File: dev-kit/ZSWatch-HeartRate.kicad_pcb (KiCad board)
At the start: 4 copper layers, 45 x 36.9 mm, 49 parts, among them IC101 LIS2DS12, IC102 MCP73832-2-OT, IC103 MAX32664, IC104 TPS61240, IC105 MAX86141, IC106 MIC5365-1.8, J101 SPI, J102 GPIO, J103 UART, J104 I2C, M101 BM15C, SW101 BTN1, SW102 RESET, X102 CHARGE, X103 BATTERY, X104 DEBUG, Y101 32kHz

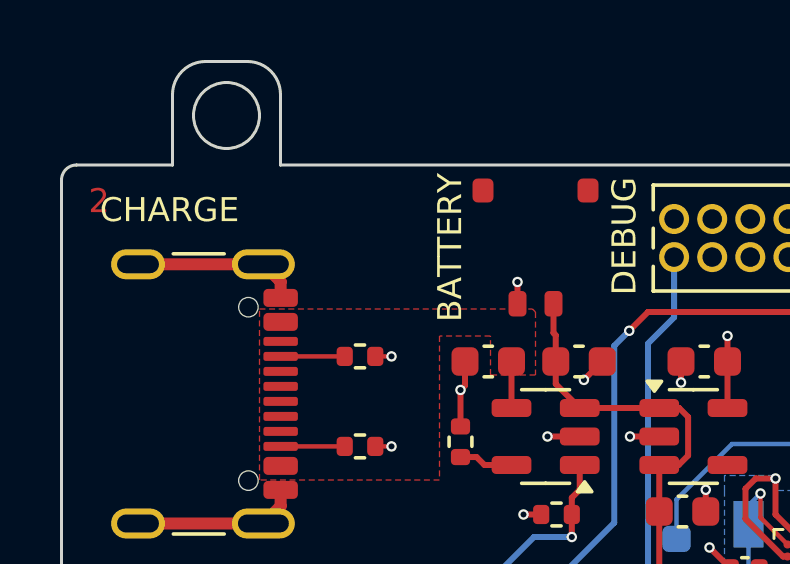
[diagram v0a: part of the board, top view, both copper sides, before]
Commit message: Start with hardware rev 3
- Fix distance between programming and battery connector

Signed-off-by: Daniel Kampert <DanielKampert@kampis-elektroecke.de>
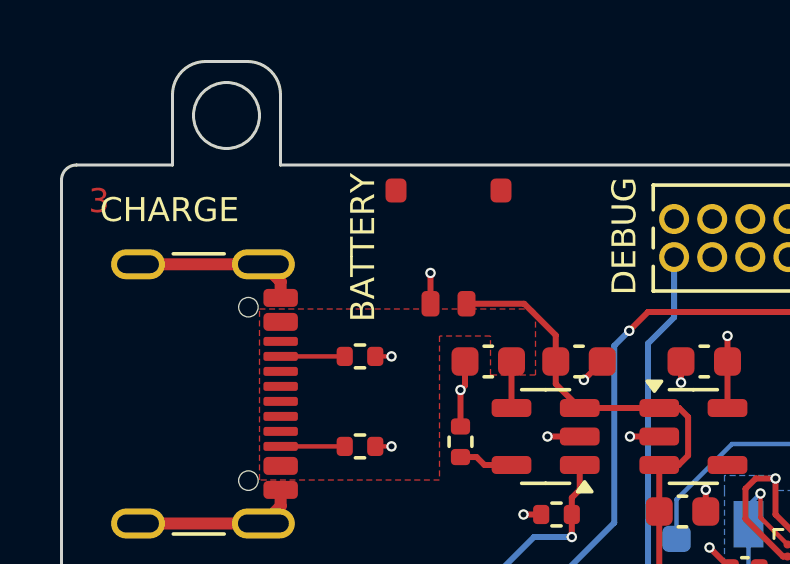
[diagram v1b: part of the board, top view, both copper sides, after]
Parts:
- moved X103 2.90 mm to (154.1, 90.5)
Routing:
- net /V_{BAT}: track 19.7 -> 22.0 mm
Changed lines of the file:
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@@
 	(paper "A4")
 	(title_block
-		(title "ZSWatch Heartrate")
-		(date "2025-04-18")
-		(rev "2")
+		(title "ZSWatch Heart Rate Dev-Board")
+		(date "2025-05-20")
+		(rev "3")
 		(company "github.com/...")
 	)
@@
 	(footprint "Molex:78171-0002"
 		(layer "F.Cu")
-		(at 157 90.55 180)
+		(at 154.1 90.55 180)
 		(descr "Molex Pico-EZmate series connector, 78171-0002 (http://www.molex.com/pdm_docs/sd/781710002_sd.pdf), generated with kicad-footprint-generator")
 		(tags "connector Molex Pico-EZmate side entry")
@@
 	)
 	(segment
-		(start 156.4 92.425)
-		(end 156.4 91.7)
-		(width 0.2)
-		(layer "F.Cu")
-		(net 1)
-	)
-	(segment
 		(start 165.92 99.25)
 		(end 165.92 98.25)
@@
 	)
 	(segment
+		(start 153.5 91.4)
+		(end 153.5 92.425)
+		(width 0.2)
+		(layer "F.Cu")
+		(net 1)
+	)
+	(segment
 		(start 168.18 103.45)
 		(end 168.18 102.75)
@@
 	)
 	(via
-		(at 156.4 91.7)
+		(at 153.5 91.4)
 		(size 0.35)
 		(drill 0.2)
@@
 	)
 	(segment
-		(start 157.675 95.1)
-		(end 158.475 95.9)
+		(start 157.675 93.475)
+		(end 157.675 94.35)
 		(width 0.2)
 		(layer "F.Cu")
@@
 	)
 	(segment
-		(start 157.6 92.425)
-		(end 157.6 93.4)
+		(start 157.675 95.1)
+		(end 158.475 95.9)
 		(width 0.2)
 		(layer "F.Cu")
@@
 	)
 	(segment
-		(start 157.675 93.475)
-		(end 157.675 94.35)
-		(width 0.2)
-		(layer "F.Cu")
-		(net 4)
-	)
-	(segment
 		(start 161.025 104.6)
 		(end 161.3 104.6)
@@
 	)
 	(segment
-		(start 157.6 93.4)
-		(end 157.675 93.475)
+		(start 154.7 92.425)
+		(end 156.625 92.425)
 		(width 0.2)
 		(layer "F.Cu")
@@
 		(width 0.2)
 		(layer "F.Cu")
+		(net 4)
+	)
+	(segment
+		(start 156.625 92.425)
+		(end 157.675 93.475)
+		(width 0.2)
+		(layer "F.Cu")

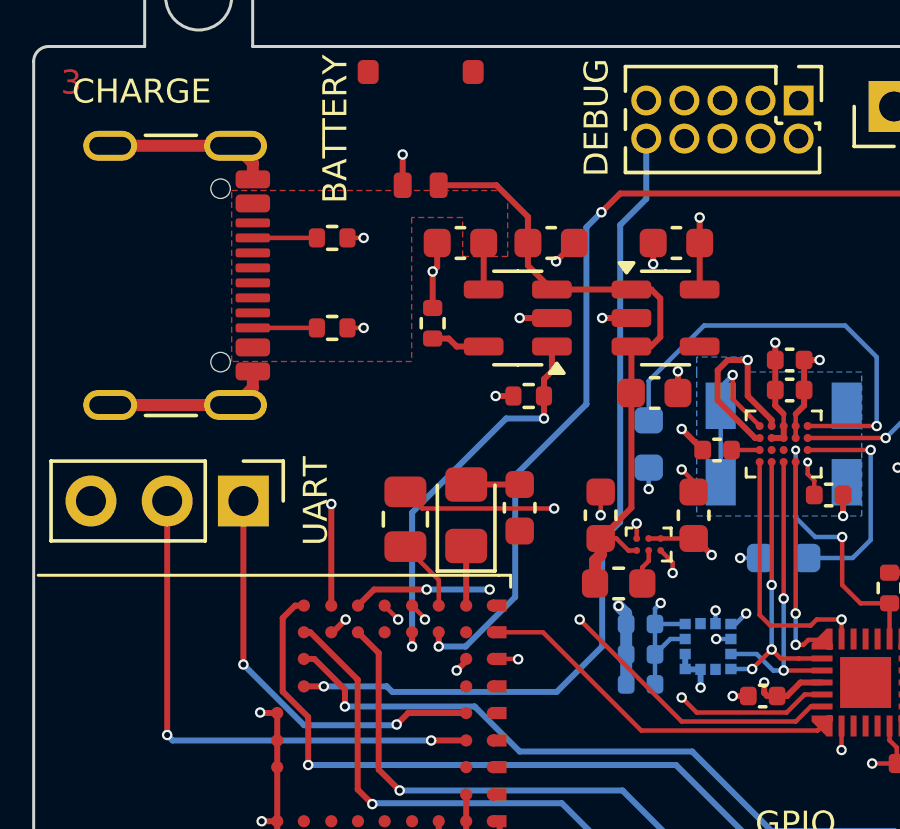
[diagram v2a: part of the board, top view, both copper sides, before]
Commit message: Bug: Issue #2
- Fix wrong circuit for the status LED

Signed-off-by: Daniel Kampert <DanielKampert@kampis-elektroecke.de>
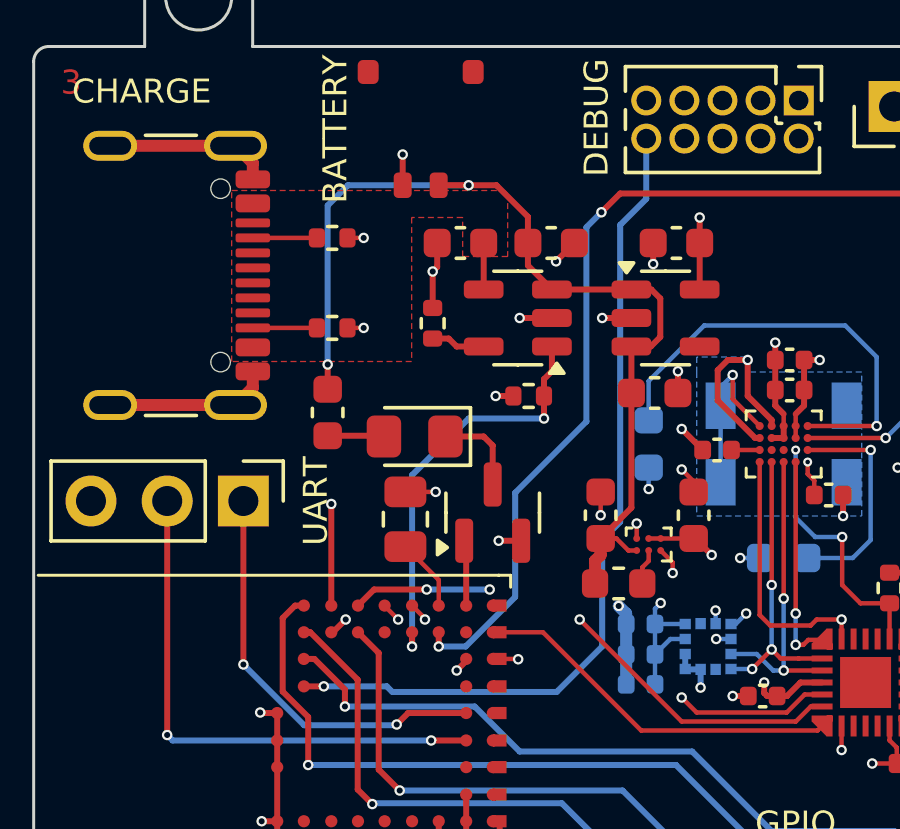
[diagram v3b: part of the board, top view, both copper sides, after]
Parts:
- added Q101: BSS138, Package_TO_SOT_SMD:SOT-23, F.Cu at (156.5, 103.3)
- moved R105 7.14 mm to (151.0, 100.0), turned to -90 degrees
- moved D107 3.14 mm to (153.9, 100.8), turned to 180 degrees
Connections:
- M101 pad K8: Net-(D107-K) -> Net-(M101-P2.05)
- R105 pad 1: +BATT -> /V_{BAT}
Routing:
- net /V_{BAT}: track 22.0 -> 33.3 mm, vias 0 -> 2
- net Net-(M101-P2.05): track 0.00 -> 2.19 mm
- net Net-(D107-K): track 1.99 -> 3.00 mm
- net GND: track 68.3 -> 69.0 mm, vias 31 -> 32
- net /CHARGE: track 13.1 -> 13.9 mm

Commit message: Issue #4
Signed-off-by: Daniel Kampert <DanielKampert@kampis-elektroecke.de>
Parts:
- moved C110 1.00 mm to (162.6, 93.3)
- moved C113 1.00 mm to (161.9, 98.3)
- moved IC106 1.00 mm to (162.3, 95.8)
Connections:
- D102 pad 2: GND -> PD_GND
- IC105 pad C5: GND -> PD_GND
- IC105 pad D4: GND -> Net-(D101-K)
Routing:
- net GND: track 69.0 -> 62.0 mm, vias 32 -> 31
- net /V_{BAT}: track 33.3 -> 34.6 mm
- net Net-(D105-K): track 14.7 -> 15.4 mm
- net Net-(D102-K): track 5.81 -> 5.19 mm
- net PD_GND: vias 0 -> 1
- added copper zone on B.Cu, net PD_GND
- added copper zone on F.Cu, net PD_GND
- added copper zone on In2.Cu, net PD_GND
- removed copper zone on In1.Cu, net (none)
- removed copper zone on B.Cu, net GND

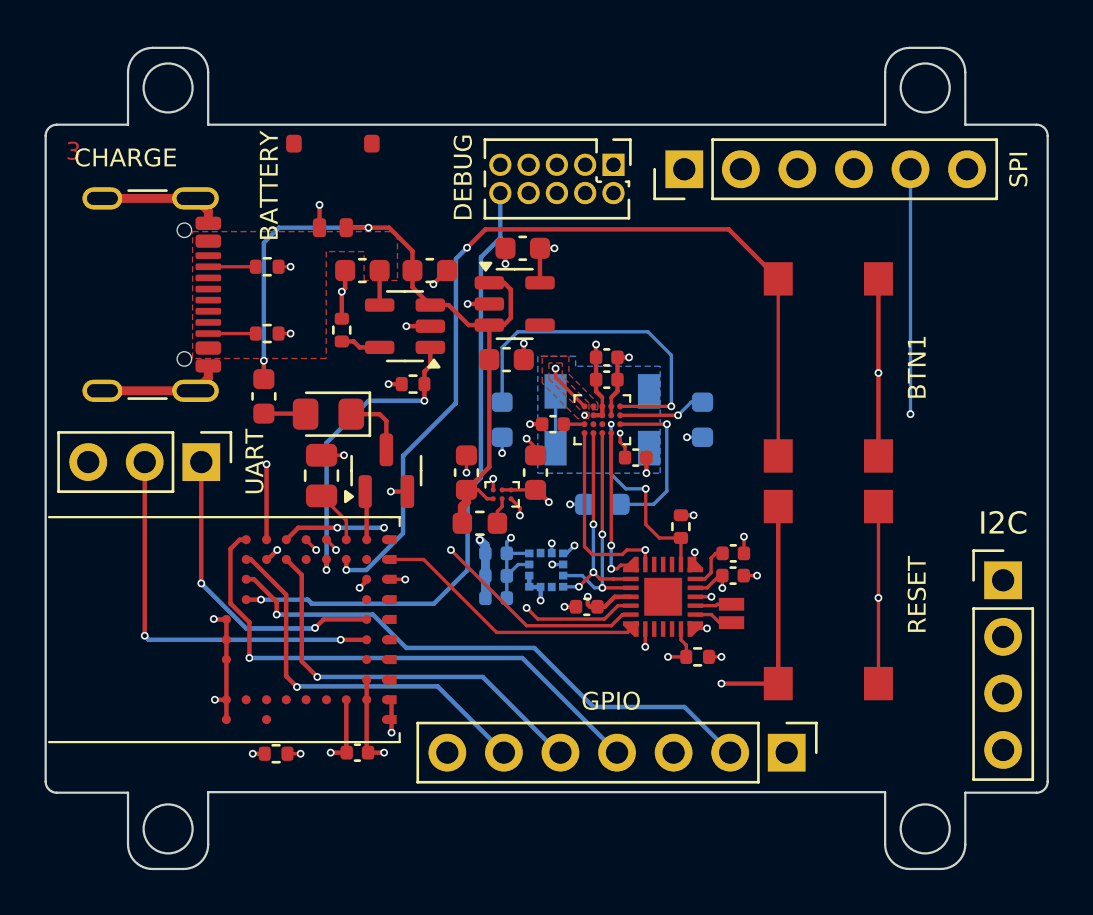
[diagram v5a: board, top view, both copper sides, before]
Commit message: Rework heartrate sensor
- Issue #7
- Issue #6
- Issue #5
- Issue #4

Signed-off-by: Daniel Kampert <DanielKampert@kampis-elektroecke.de>
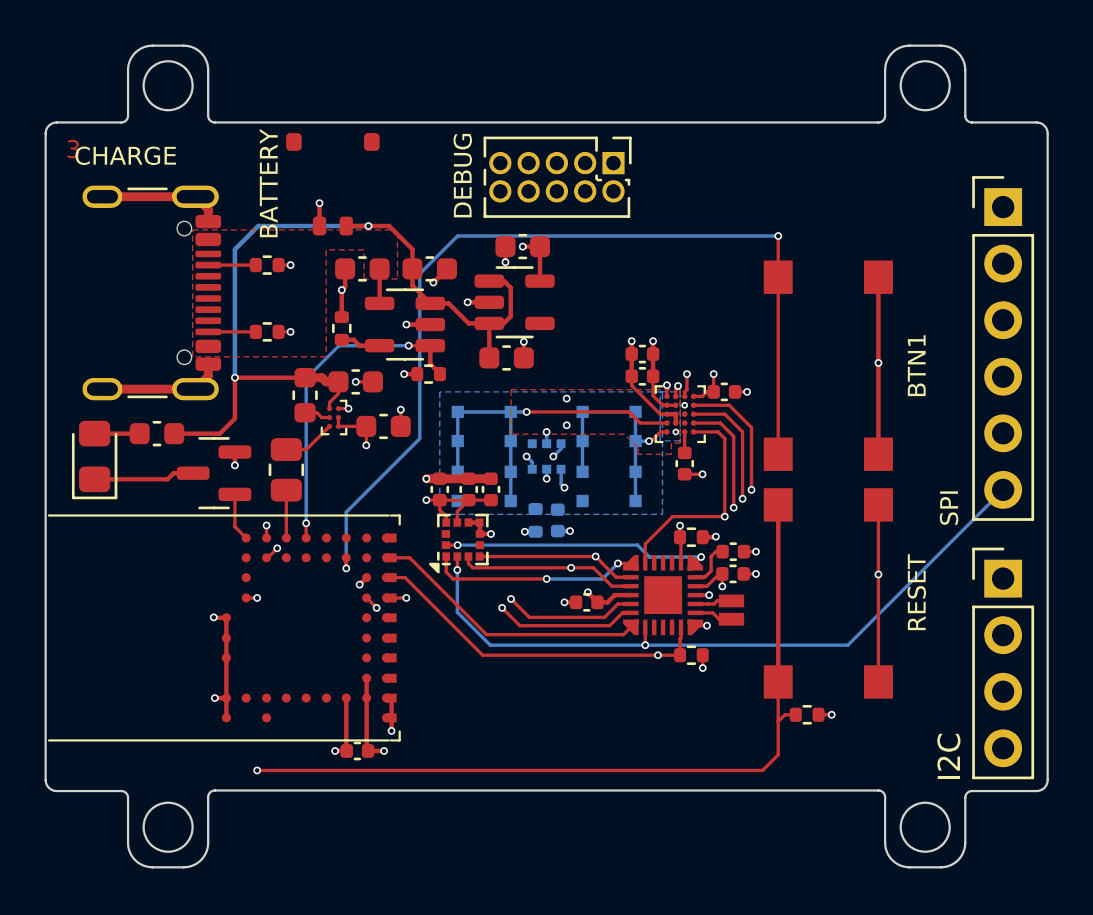
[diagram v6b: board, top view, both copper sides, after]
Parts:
- removed D104: IR, Diode_SMD:D_0603_1608Metric
- removed D105: GREEN, Diode_SMD:D_0603_1608Metric
- removed D106: RED, Diode_SMD:D_0603_1608Metric
- removed J102: GPIO, Connector_PinHeader_2.54mm:PinHeader_1x07_P2.54mm_Vertical
- removed J103: UART, Connector_PinHeader_2.54mm:PinHeader_1x03_P2.54mm_Vertical
- added C118: ~, Capacitor_SMD:C_0402_1005Metric, B.Cu at (164.2, 105.6)
- added D101: D_Photo, Vishay:VEMD8080, B.Cu at (160.9, 102.7)
- added LED101: SFH 7016, Osram:SFH7016, B.Cu at (163.7, 102.7)
- added R110: ~, Resistor_SMD:R_0402_1005Metric, B.Cu at (163.2, 105.6)
- C114, C115, C116, IC101: moved to F.Cu
- D102: footprint Vishay:VEMD5080X01 -> Vishay:VEMD8080
- moved R108 23.9 mm to (175.4, 114.3)
- moved J101 14.4 mm to (184.2, 91.5), turned to 0 degrees
- moved D107 10.7 mm to (143.4, 102.7), turned to 90 degrees
- moved L101 9.73 mm to (152.8, 100.0), turned to -90 degrees
- moved IC104 8.30 mm to (154.2, 101.0), turned to 0 degrees
- moved Q101 7.74 mm to (148.8, 103.5), turned to 180 degrees
- moved C108 7.13 mm to (156.4, 101.3), turned to 0 degrees
- moved C107 6.43 mm to (155.1, 99.3), turned to 0 degrees
- moved C104 6.18 mm to (169.9, 103.0), turned to -90 degrees
- moved R105 5.08 mm to (146.2, 101.7), turned to 180 degrees
- moved C106 4.95 mm to (171.7, 99.8)
- moved C115 4.89 mm to (161.2, 104.2), turned to 90 degrees
- moved C114 4.07 mm to (160.2, 104.2), turned to 90 degrees
- moved IC101 3.99 mm to (159.9, 106.4), turned to 90 degrees
- moved C116 3.83 mm to (158.9, 104.2), turned to 90 degrees
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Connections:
- J101 pad 2: Net-(IC101-SDA/SDI/SDO) -> Net-(IC101-SCL/SCLK)
- J101 pad 4: Net-(IC101-SCL/SCLK) -> Net-(IC101-SDA/SDI/SDO)
- J101 pad 5: Net-(IC101-CS) -> Net-(IC103-CS_{PPG})
- J101 pad 6: Net-(IC103-CS_{PPG}) -> Net-(IC101-CS)
- M101 pad E8: /TxD -> unconnected-(M101-P1.03/NFC-PadE8)
- M101 pad F8: Net-(J103-Pin_1) -> unconnected-(M101-P1.05/AIN1-PadF8)
- M101 pad G8: unconnected-(M101-P1.08-PadG8) -> /SCL
- M101 pad G9: unconnected-(M101-P1.07/AIN3-PadG9) -> /SDA
- M101 pad H2: Net-(J102-Pin_2) -> unconnected-(M101-P0.04-PadH2)
- M101 pad J2: Net-(J102-Pin_6) -> unconnected-(M101-P0.03-PadJ2)
- M101 pad J4: Net-(J102-Pin_5) -> unconnected-(M101-P0.00-PadJ4)
- M101 pad J6: /CHARGE -> unconnected-(M101-P2.07-PadJ6)
- M101 pad K2: Net-(J102-Pin_4) -> Net-(M101-P0.02)
- M101 pad K4: Net-(J102-Pin_3) -> Net-(M101-P0.01)
- M101 pad K5: /SDA -> /CHARGE
- M101 pad K6: /SCL -> unconnected-(M101-P2.08-PadK6)
- M101 pad K7: Net-(M101-P2.06) -> unconnected-(M101-P2.06-PadK7)
- M101 pad K8: Net-(M101-P2.05) -> unconnected-(M101-P2.05-PadK8)
- Q101 pad 1: Net-(M101-P2.05) -> Net-(M101-P0.02)
- R109 pad 1: Net-(M101-P2.06) -> Net-(M101-P0.01)
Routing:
- net Net-(J102-Pin_3): track 25.4 -> 0.00 mm, vias 2 -> 0
- net Net-(J102-Pin_2): track 25.3 -> 0.00 mm, vias 1 -> 0
- net Net-(J102-Pin_4): track 24.4 -> 0.00 mm, vias 1 -> 0
- net Net-(J102-Pin_5): track 18.2 -> 0.00 mm, vias 1 -> 0
- net /TxD: track 17.8 -> 0.00 mm, vias 2 -> 0
- net Net-(J102-Pin_6): track 17.3 -> 0.00 mm, vias 1 -> 0
- net Net-(D101-K): track 0.00 -> 16.3 mm, vias 0 -> 1
- net Net-(J103-Pin_1): track 13.9 -> 0.00 mm, vias 2 -> 0
- net Net-(IC101-SCL/SCLK): track 31.3 -> 41.6 mm
- net /ENABLE_{LED}: track 10.9 -> 2.37 mm, vias 2 -> 0
- net Net-(IC101-CS): track 39.7 -> 31.3 mm, vias 3 -> 2
- net /SCL: track 43.6 -> 35.6 mm
- net Net-(IC103-CS_{PPG}): track 31.8 -> 24.0 mm
- net Net-(IC105-LED1_DRV): track 15.4 -> 8.06 mm, vias 1 -> 2
- net Net-(IC101-SDO/ADDR0): track 31.0 -> 37.6 mm
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- added copper zone on In1.Cu, net +1V8
- added copper zone on In1.Cu, net /V_{LED}
- added copper zone on In2.Cu, net GND
- removed copper zone on In2.Cu, net +1V8
- removed copper zone on In2.Cu, net /V_{LED}
- removed copper zone on In1.Cu, net GND
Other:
- outline, holes or cut-outs redrawn

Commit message: Issue #8
Signed-off-by: Daniel Kampert <DanielKampert@kampis-elektroecke.de>
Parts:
- D101, D102: footprint Vishay:VEMD8080 -> Vishay:VEMD808x
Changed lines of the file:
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@@
 		)
 	)
-	(footprint "Vishay:VEMD8080"
+	(footprint "Vishay:VEMD808x"
 		(layer "B.Cu")
 		(at 166.5 102.7 -90)
@@
 			(unlocked yes)
 			(layer "B.SilkS")
-			(hide yes)
 			(effects
 				(font
@@
 			(unlocked yes)
 			(layer "B.Fab")
-			(hide yes)
-			(effects
-				(font
-					(size 1 1)
-					(thickness 0.15)
-				)
-				(justify mirror)
-			)
-		)
-		(property "Datasheet" "https://www.vishay.com/doc?84565"
+			(effects
+				(font
+					(size 1 1)
+					(thickness 0.15)
+				)
+				(justify mirror)
+			)
+		)
+		(property "Datasheet" "https://www.vishay.com/docs/80381/vemd8082.pdf"
 			(at 0 0 90)
 			(unlocked yes)
@@
 			)
 		)
-		(property "manf#" "VEMD8080"
+		(property "manf#" "VEMD8082"
 			(at 0 0 270)
 			(unlocked yes)
@@
 			)
 		)
-		(property "mouser#" "78-VEMD8080"
+		(property "mouser#" "78-VEMD8082"
 			(at 0 0 270)
 			(unlocked yes)
@@
 		)
 	)
-	(footprint "Vishay:VEMD8080"
+	(footprint "Vishay:VEMD808x"
 		(layer "B.Cu")
 		(at 160.9 102.7 -90)
@@
 			(unlocked yes)
 			(layer "B.SilkS")
-			(hide yes)
 			(effects
 				(font
@@
 			(unlocked yes)
 			(layer "B.Fab")
-			(hide yes)
-			(effects
-				(font
-					(size 1 1)
-					(thickness 0.15)
-				)
-				(justify mirror)
-			)
-		)
-		(property "Datasheet" "https://www.vishay.com/doc?84565"
+			(effects
+				(font
+					(size 1 1)
+					(thickness 0.15)
+				)
+				(justify mirror)
+			)
+		)
+		(property "Datasheet" "https://www.vishay.com/docs/80381/vemd8082.pdf"
 			(at 0 0 90)
 			(unlocked yes)
@@
 		)
 		(property "manf" "Vishay Semiconductors"
-			(at 0 0 90)
-			(unlocked yes)
-			(layer "B.Fab")
-			(hide yes)
-			(effects
-				(font
-					(size 0.8 0.8)
-					(thickness 0.12)
-				)
-				(justify mirror)
-			)
-		)
-		(property "manf#" "VEMD8080"
-			(at 0 0 90)
-			(unlocked yes)
-			(layer "B.Fab")
-			(hide yes)
-			(effects
-				(font
-					(size 0.8 0.8)
-					(thickness 0.12)
-				)
-				(justify mirror)
-			)
-		)
-		(property "mouser#" "78-VEMD8080"
-			(at 0 0 90)
+			(at 0 0 270)
+			(unlocked yes)
+			(layer "B.Fab")
+			(hide yes)
+			(effects
+				(font
+					(size 0.8 0.8)
+					(thickness 0.12)
+				)
+				(justify mirror)
+			)
+		)
+		(property "manf#" "VEMD8082"
+			(at 0 0 270)
+			(unlocked yes)
+			(layer "B.Fab")
+			(hide yes)
+			(effects
+				(font
+					(size 0.8 0.8)
+					(thickness 0.12)
+				)
+				(justify mirror)
+			)
+		)
+		(property "mouser#" "78-VEMD8082"
+			(at 0 0 270)
 			(unlocked yes)
 			(layer "B.Fab")
@@
 		)
 		(property "CONFIG" ""
-			(at 0 0 90)
-			(unlocked yes)
-			(layer "B.Fab")
+			(at 0 0 270)
+			(unlocked yes)
+			(layer "B.Fab")
